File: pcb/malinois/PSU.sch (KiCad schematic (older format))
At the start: 3 parts

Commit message: charger started
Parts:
- removed U?: TP4056, symbol psu:TP4056
- removed U?: DW01A, symbol psu:DW01A
- removed U?: FS8205A, symbol psu:FS8205A
- added C? (x3): C_Small, symbol Device:C_Small
- added R?: 1k, symbol Device:R_Small
- added R?: R_Small, symbol Device:R_Small
- added R?: 100, symbol Device:R_Small
- added U?: FS8205A, symbol psu:FS8205A
- added U?: TP4056, symbol psu:TP4056
- added U?: DW01A, symbol psu:DW01A
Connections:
- net labels added: GND
- wire segments 0 -> 26
- no-connect marks 0 -> 2
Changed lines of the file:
@@
 $EndDescr
 $Comp
-L psu:TP4056 U?
-U 1 1 5E6AF281
-P 2950 3275
-F 0 "U?" H 2925 3890 50  0000 C CNN
-F 1 "TP4056" H 2925 3799 50  0000 C CNB
-F 2 "" H 2950 3275 50  0001 C CNN
-F 3 "" H 2950 3275 50  0001 C CNN
-	1    2950 3275
+L Device:C_Small C?
+U 1 1 5E6B19E5
+P 2100 2900
+F 0 "C?" H 2192 2946 50  0000 L CNN
+F 1 "C_Small" H 2192 2855 50  0000 L CNN
+F 2 "" H 2100 2900 50  0001 C CNN
+F 3 "~" H 2100 2900 50  0001 C CNN
+	1    2100 2900
 	1    0    0    -1
 $EndComp
 $Comp
-L psu:DW01A U?
-U 1 1 5E6AF8A4
-P 5125 2600
-F 0 "U?" H 5150 3065 50  0000 C CNN
-F 1 "DW01A" H 5150 2974 50  0000 C CNB
-F 2 "" H 5125 2600 50  0001 C CNN
-F 3 "" H 5125 2600 50  0001 C CNN
-	1    5125 2600
+L Device:C_Small C?
+U 1 1 5E6B3CC2
+P 7500 2500
+F 0 "C?" H 7592 2546 50  0000 L CNN
+F 1 "C_Small" H 7592 2455 50  0000 L CNN
+F 2 "" H 7500 2500 50  0001 C CNN
+F 3 "~" H 7500 2500 50  0001 C CNN
+	1    7500 2500
 	1    0    0    -1
 $EndComp
 $Comp
+L Device:R_Small R?
+U 1 1 5E6B63AF
+P 4500 3700
+F 0 "R?" H 4559 3746 50  0000 L CNN
+F 1 "1k" H 4559 3655 50  0000 L CNN
+F 2 "" H 4500 3700 50  0001 C CNN
+F 3 "~" H 4500 3700 50  0001 C CNN
+	1    4500 3700
+	1    0    0    -1
+$EndComp
+Wire Wire Line
+	5450 2900 5450 2975
+Wire Wire Line
+	5450 2975 5550 2975
+Wire Wire Line
+	5550 2975 5550 3375
+Wire Wire Line
+	4850 2900 4850 2975
+Wire Wire Line
+	4850 2975 4750 2975
+Wire Wire Line
+	4750 2975 4750 3375
+$Comp
 L psu:FS8205A U?
-U 1 1 5E6AFB5F
+U 1 1 5E6C013A
 P 5150 3900
-F 0 "U?" H 5769 4084 50  0000 L CNN
-F 1 "FS8205A" H 5769 3993 50  0000 L CNN
+F 0 "U?" H 4850 4400 50  0000 L CNB
+F 1 "FS8205A" H 5000 4250 50  0000 L CNB
 F 2 "" H 5100 3850 50  0001 C CNN
 F 3 "" H 5100 3850 50  0001 C CNN
@@
 	1    0    0    -1
 $EndComp
+Wire Wire Line
+	4500 3600 4500 2550
+Wire Wire Line
+	4500 2550 4600 2550
+Wire Wire Line
+	4500 3800 4500 4000
+Wire Wire Line
+	4500 4000 4600 4000
+$Comp
+L power:GND #PWR?
+U 1 1 5E6C74EE
+P 4500 4150
+F 0 "#PWR?" H 4500 3900 50  0001 C CNN
+F 1 "GND" H 4505 3977 50  0000 C CNN
+F 2 "" H 4500 4150 50  0001 C CNN
+F 3 "" H 4500 4150 50  0001 C CNN
+	1    4500 4150
+	1    0    0    -1
+$EndComp
+NoConn ~ 5100 4150
+NoConn ~ 5200 4150
+Wire Wire Line
+	4500 4150 4500 4000
+Connection ~ 4500 4000
+$Comp
+L Device:C_Small C?
+U 1 1 5E6C802F
+P 5750 2450
+F 0 "C?" H 5842 2496 50  0000 L CNN
+F 1 "C_Small" H 5842 2405 50  0000 L CNN
+F 2 "" H 5750 2450 50  0001 C CNN
+F 3 "~" H 5750 2450 50  0001 C CNN
+	1    5750 2450
+	1    0    0    -1
+$EndComp
+Wire Wire Line
+	5650 2300 5750 2300
+Wire Wire Line
+	5750 2300 5750 2350
+Wire Wire Line
+	5750 2550 5650 2550
+Wire Wire Line
+	5700 4000 5750 4000
+Wire Wire Line
+	5750 4000 5750 2550
+Connection ~ 5750 2550
+$Comp
+L psu:TP4056 U?
+U 1 1 5E6CE750
+P 3500 2600
+F 0 "U?" H 3475 3465 50  0000 C CNN
+F 1 "TP4056" H 3475 3374 50  0000 C CNB
+F 2 "" H 3500 2600 50  0001 C CNN
+F 3 "" H 3500 2600 50  0001 C CNN
+	1    3500 2600
+	1    0    0    -1
+$EndComp
+Wire Wire Line
+	3850 2000 6200 2000
+Wire Wire Line
+	3850 3100 3850 3600
+Wire Wire Line
+	3850 3600 3500 3600
+Wire Wire Line
+	3500 3600 3500 3450
+$Comp
+L power:GND #PWR?
+U 1 1 5E6D210D
+P 3500 3700
+F 0 "#PWR?" H 3500 3450 50  0001 C CNN
+F 1 "GND" H 3505 3527 50  0000 C CNN
+F 2 "" H 3500 3700 50  0001 C CNN
+F 3 "" H 3500 3700 50  0001 C CNN
+	1    3500 3700
+	1    0    0    -1
+$EndComp
+Wire Wire Line
+	3500 3700 3500 3600
+Connection ~ 3500 3600
+Wire Wire Line
+	3850 2950 4000 2950
+Wire Wire Line
+	4000 2950 4000 3300
+$Comp
+L Device:R_Small R?
+U 1 1 5E6D5971
+P 4000 3400
+F 0 "R?" H 4059 3446 50  0000 L CNN
+F 1 "R_Small" H 4059 3355 50  0000 L CNN
+F 2 "" H 4000 3400 50  0001 C CNN
+F 3 "~" H 4000 3400 50  0001 C CNN
+	1    4000 3400
+	1    0    0    -1
+$EndComp
+$Comp
+L power:GND #PWR?
+U 1 1 5E6D5E55
+P 4000 3700
+F 0 "#PWR?" H 4000 3450 50  0001 C CNN
+F 1 "GND" H 4005 3527 50  0000 C CNN
+F 2 "" H 4000 3700 50  0001 C CNN
+F 3 "" H 4000 3700 50  0001 C CNN
+	1    4000 3700
+	1    0    0    -1
+$EndComp
+Wire Wire Line
+	4000 3500 4000 3700
+Wire Wire Line
+	5750 4000 6250 4000
+Connection ~ 5750 4000
+Wire Wire Line
+	5750 2300 6350 2300
+Connection ~ 5750 2300
+$Comp
+L psu:DW01A U?
+U 1 1 5E6DD81F
+P 5200 2600
+F 0 "U?" H 4750 3100 50  0000 C CNN
+F 1 "DW01A" H 5150 2750 50  0000 C CNB
+F 2 "" H 5200 2600 50  0001 C CNN
+F 3 "" H 5200 2600 50  0001 C CNN
+	1    5200 2600
+	1    0    0    -1
+$EndComp
+$Comp
+L Device:R_Small R?
+U 1 1 5E6DEBE9
+P 6450 2300
+F 0 "R?" V 6254 2300 50  0000 C CNN
+F 1 "100" V 6345 2300 50  0000 C CNN
+F 2 "" H 6450 2300 50  0001 C CNN
+F 3 "~" H 6450 2300 50  0001 C CNN
+	1    6450 2300
+	0    1    1    0
+$EndComp
 $EndSCHEMATC

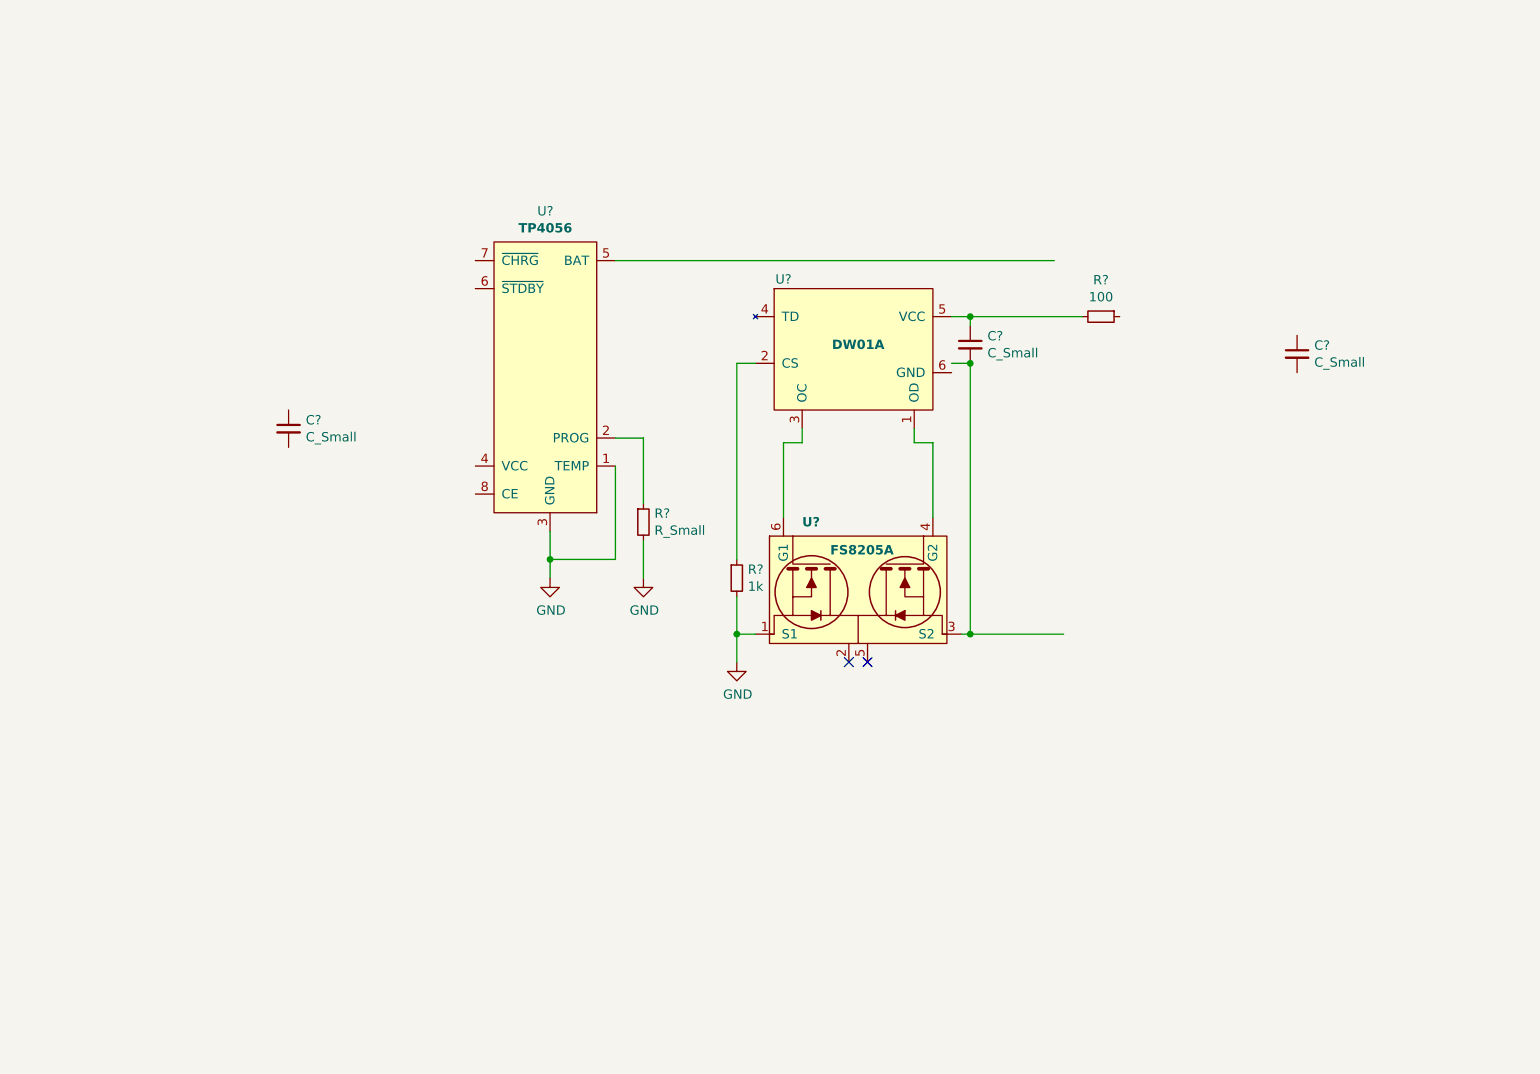
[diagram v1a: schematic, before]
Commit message: 5V boost
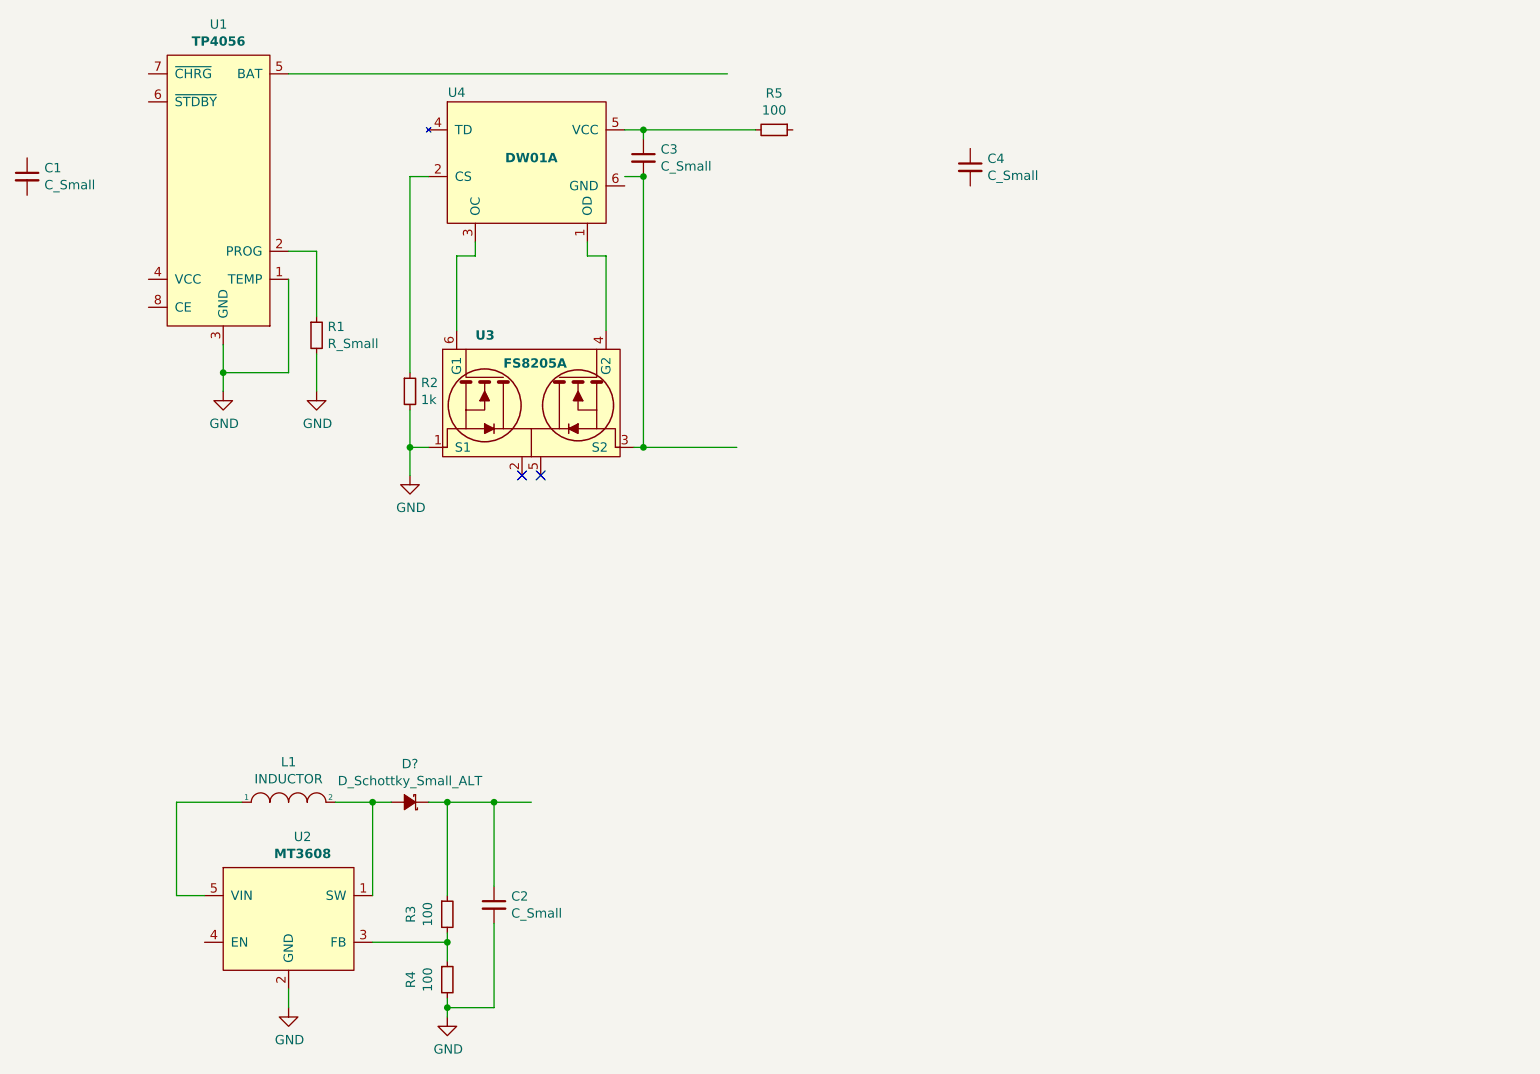
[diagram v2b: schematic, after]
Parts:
- added C2: C_Small, symbol Device:C_Small
- added D?: D_Schottky_Small_ALT, symbol Device:D_Schottky_Small_ALT
- added L1: INDUCTOR, symbol pspice:INDUCTOR
- added R3, R4: 100, symbol Device:R_Small
- added U2: MT3608, symbol psu:MT3608
- gave numbers to parts that had none: 9
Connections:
- wire segments 26 -> 45
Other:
- moved on the sheet: C1, C3, C4, R1, R2, R5, U1, U3, U4

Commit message: wiring PSU
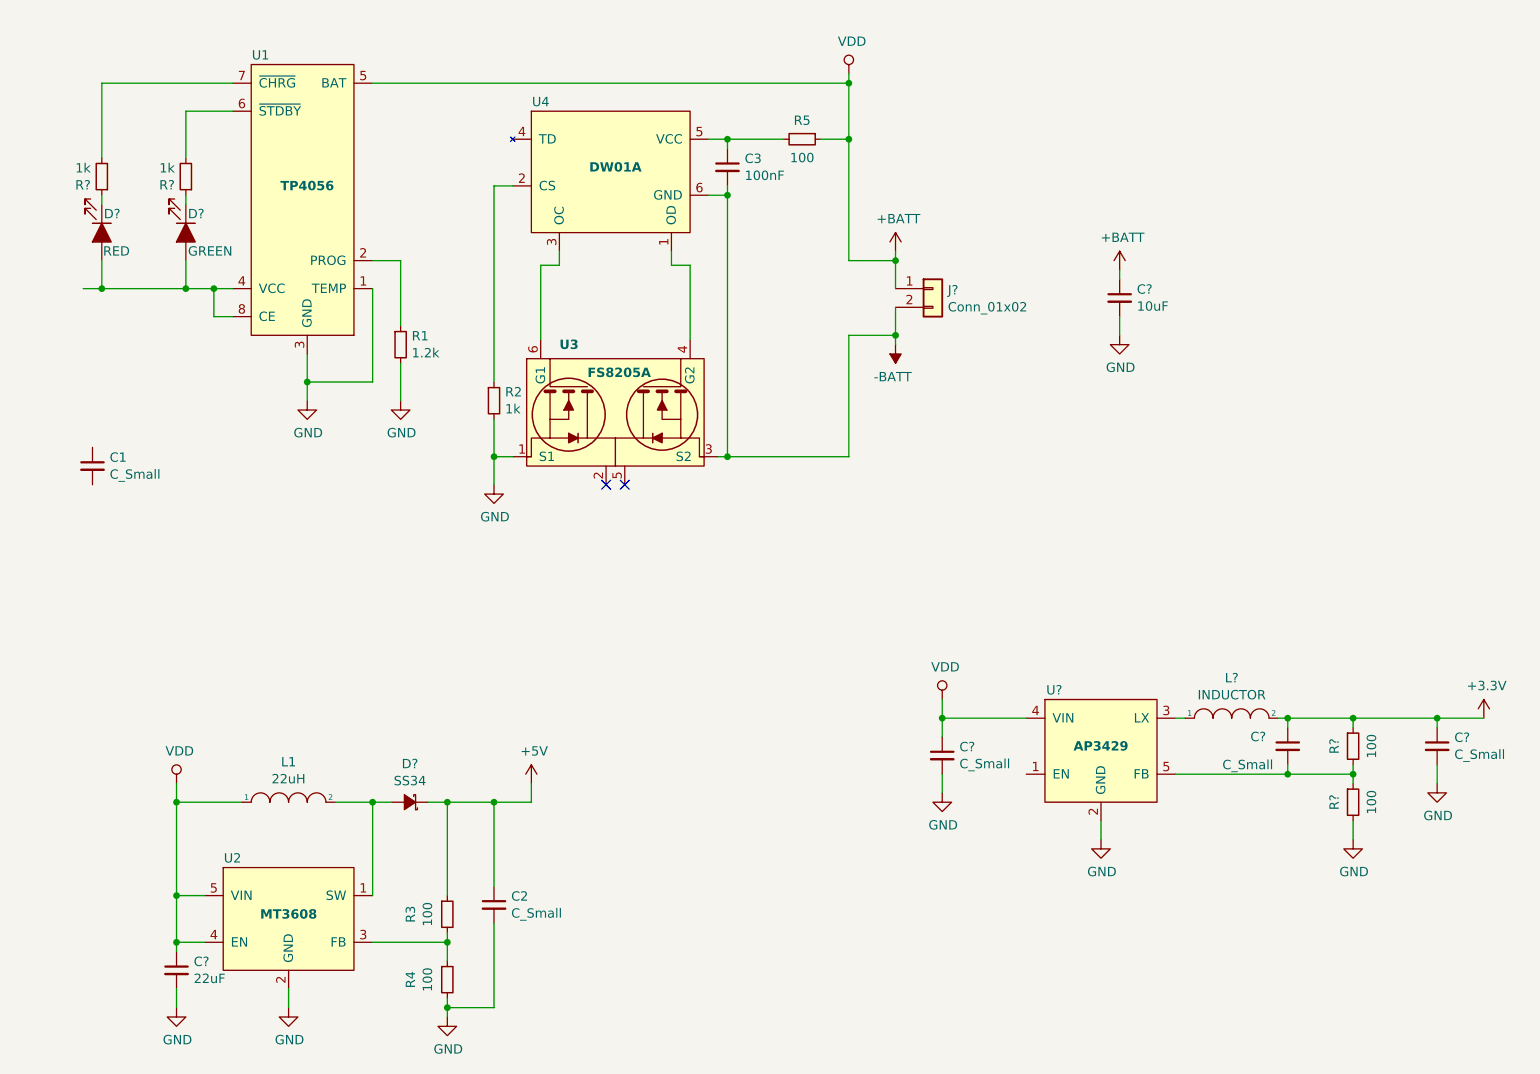
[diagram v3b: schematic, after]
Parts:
- removed C4: C_Small, symbol Device:C_Small
- added C? (x3): C_Small, symbol Device:C_Small
- added C?: 10uF, symbol Device:C_Small
- added C?: 22uF, symbol Device:C_Small
- added D?: GREEN, symbol Device:LED_ALT
- added D?: RED, symbol Device:LED_ALT
- added J?: Conn_01x02, symbol Connector_Generic:Conn_01x02
- added L?: INDUCTOR, symbol pspice:INDUCTOR
- added R? (x2): 100, symbol Device:R_Small
- added R? (x2): 1k, Resistor_SMD:R_0402_1005Metric, symbol Device:R_Small
- added U?: AP3429, symbol psu:AP3429
- C3: value C_Small -> 100nF
- D?: value D_Schottky_Small_ALT -> SS34
- L1: value INDUCTOR -> 22uH
- R1: value R_Small -> 1.2k; footprint (none) -> Resistor_SMD:R_0402_1005Metric
- R2, R5: footprint (none) -> Resistor_SMD:R_0402_1005Metric
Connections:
- net labels added: +3.3V, +5V, +BATT, -BATT, VDD
- wire segments 45 -> 99
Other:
- moved on the sheet: C1, C3, R1, R2, R5, U1, U3, U4
